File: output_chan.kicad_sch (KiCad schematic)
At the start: 12 parts, among them U4 MAX14917AFM+

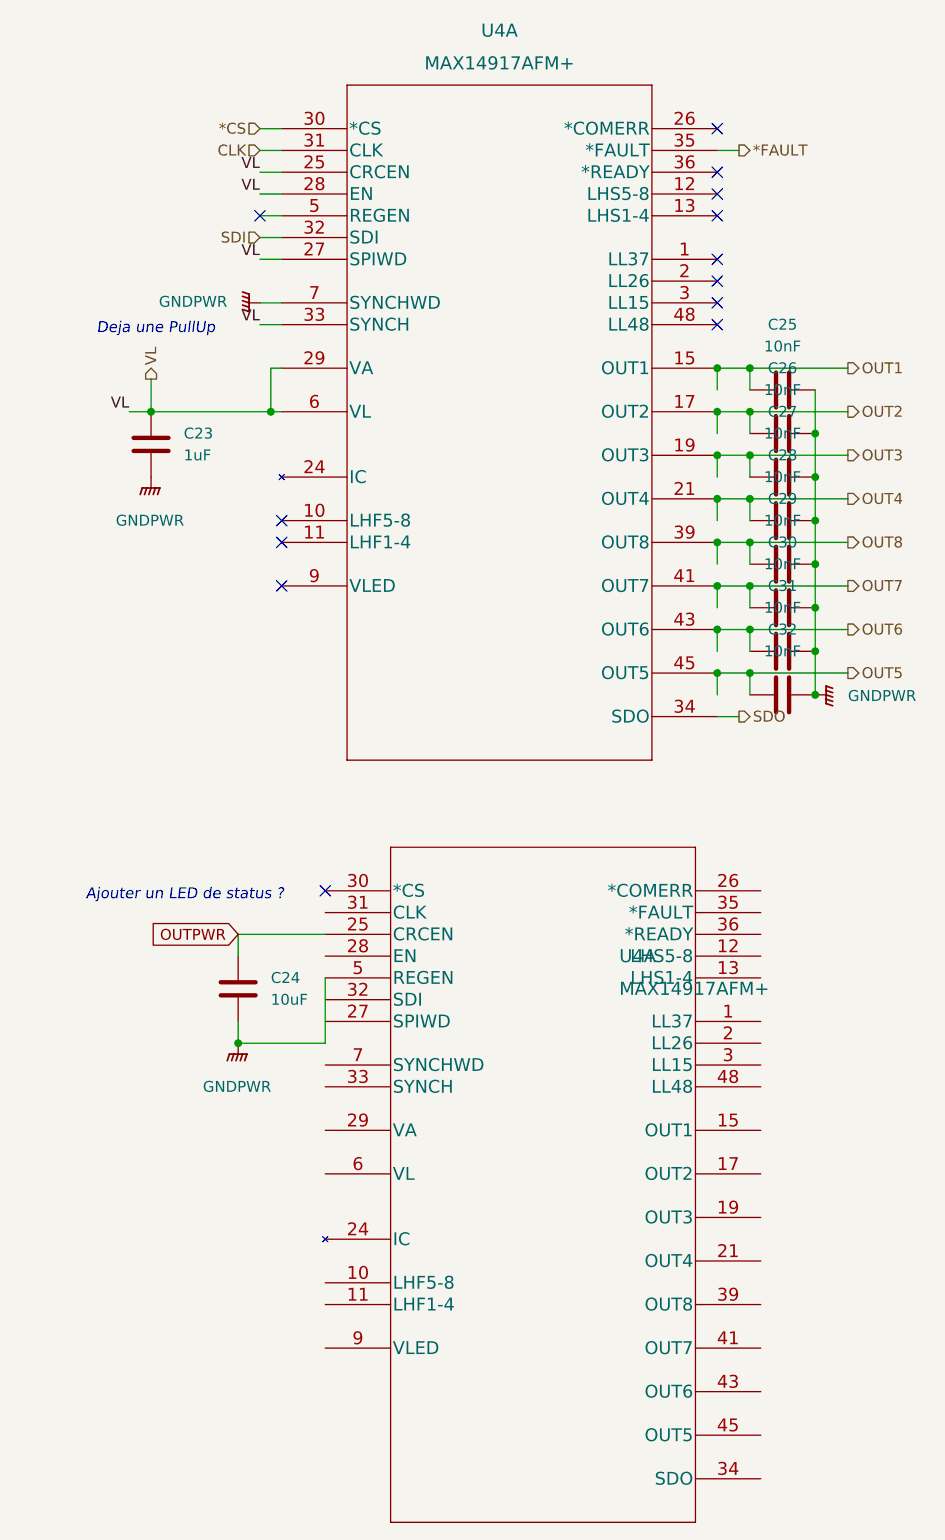
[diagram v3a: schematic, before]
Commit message: fixes after V1
4 resistors for input power
disable CRCEN
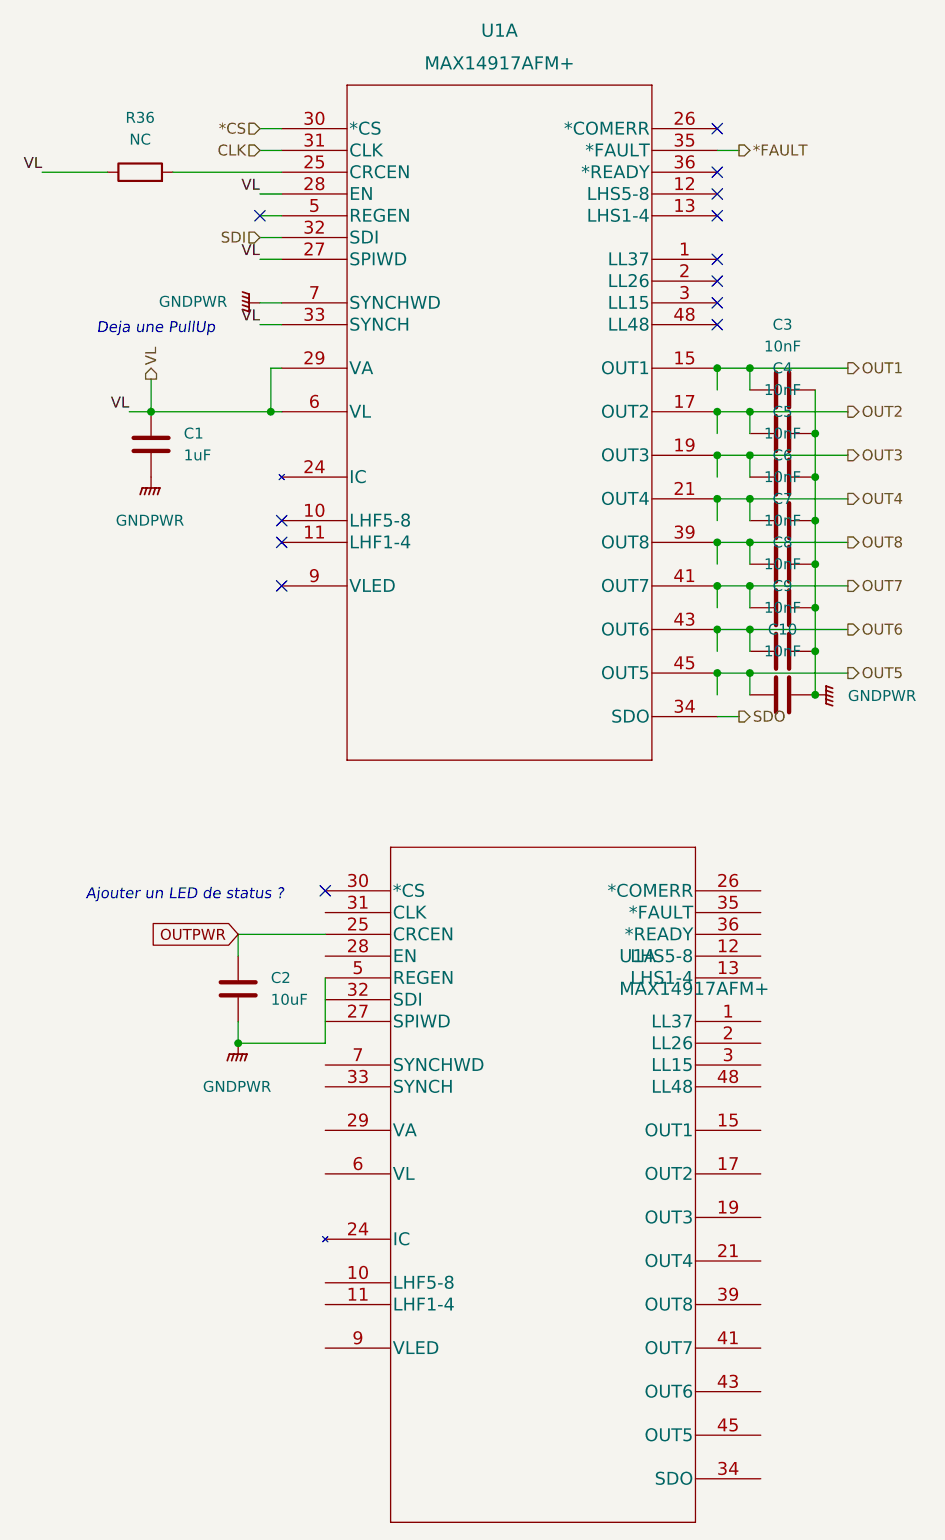
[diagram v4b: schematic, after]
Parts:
- added R36: NC, Resistor_SMD:R_0603_1608Metric, symbol Device:R
- renumbered C23 to C1, C32 to C10, C24 to C2, C25 to C3, C26 to C4, C27 to C5, C28 to C6, C29 to C7, C30 to C8, C31 to C9, U4 to U1
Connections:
- net VL: now also R36.1; no longer U1.25 (CRCEN)
- new net: R36.2, U1.25 (CRCEN)
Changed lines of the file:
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@@
+    (stroke (width 0) (type default) (color 0 0 0 0))
+  )
+  (wire (pts (xy 99.06 48.26) (xy 106.68 48.26))
     (stroke (width 0) (type default) (color 0 0 0 0))
   )
@@
     (stroke (width 0) (type default) (color 0 0 0 0))
   )
+  (wire (pts (xy 114.3 48.26) (xy 127 48.26))
+    (stroke (width 0) (type default) (color 0 0 0 0))
+  )
   (wire (pts (xy 181.61 101.6) (xy 181.61 104.14))
     (stroke (width 0) (type default) (color 0 0 0 0))
@@
   )
   (wire (pts (xy 177.8 96.52) (xy 177.8 99.06))
-    (stroke (width 0) (type default) (color 0 0 0 0))
-  )
-  (wire (pts (xy 124.46 48.26) (xy 127 48.26))
     (stroke (width 0) (type default) (color 0 0 0 0))
   )
@@
     (effects (font (size 1.27 1.27)) (justify right bottom))
   )
-  (label "VL" (at 124.46 48.26 180)
+  (label "VL" (at 99.06 48.26 180)
     (effects (font (size 1.27 1.27)) (justify right bottom))
   )
@@
   (symbol (lib_id "Device:C") (at 111.76 80.01 0)
     (in_bom yes) (on_board yes) (fields_autoplaced)
-    (property "Reference" "C23" (id 0) (at 115.57 78.7399 0)
+    (property "Reference" "C1" (id 0) (at 115.57 78.7399 0)
       (effects (font (size 1.27 1.27)) (justify left))
     )
@@
   (symbol (lib_id "Maxim industrial IO:MAX14917AFM+") (at 127 43.18 0)
     (in_bom yes) (on_board yes) (fields_autoplaced)
-    (property "Reference" "U4" (id 0) (at 152.4 31.75 0)
+    (property "Reference" "U1" (id 0) (at 152.4 31.75 0)
       (effects (font (size 1.524 1.524)))
     )
@@
   (symbol (lib_id "Device:C") (at 185.42 83.82 90)
     (in_bom yes) (on_board yes) (fields_autoplaced)
-    (property "Reference" "C27" (id 0) (at 185.42 76.2 90))
+    (property "Reference" "C5" (id 0) (at 185.42 76.2 90))
     (property "Value" "10nF" (id 1) (at 185.42 78.74 90))
     (property "Footprint" "Capacitor_SMD:C_0603_1608Metric" (id 2) (at 189.23 82.8548 0)
@@
     (pin "2")
   )
+  (symbol (lib_id "Device:R") (at 110.49 48.26 90)
+    (in_bom yes) (on_board yes) (fields_autoplaced)
+    (property "Reference" "R36" (id 0) (at 110.49 41.91 90))
+    (property "Value" "NC" (id 1) (at 110.49 44.45 90))
+    (property "Footprint" "Resistor_SMD:R_0603_1608Metric" (id 2) (at 110.49 50.038 90)
+      (effects (font (size 1.27 1.27)) hide)
+    )
+    (property "Datasheet" "~" (id 3) (at 110.49 48.26 0)
+      (effects (font (size 1.27 1.27)) hide)
+    )
+    (pin "1")
+    (pin "2")
+  )
   (symbol (lib_id "Device:C") (at 185.42 88.9 90)
     (in_bom yes) (on_board yes) (fields_autoplaced)
-    (property "Reference" "C28" (id 0) (at 185.42 81.28 90))
+    (property "Reference" "C6" (id 0) (at 185.42 81.28 90))
     (property "Value" "10nF" (id 1) (at 185.42 83.82 90))
     (property "Footprint" "Capacitor_SMD:C_0603_1608Metric" (id 2) (at 189.23 87.9348 0)
@@
   (symbol (lib_id "Device:C") (at 185.42 78.74 90)
     (in_bom yes) (on_board yes) (fields_autoplaced)
-    (property "Reference" "C26" (id 0) (at 185.42 71.12 90))
+    (property "Reference" "C4" (id 0) (at 185.42 71.12 90))
     (property "Value" "10nF" (id 1) (at 185.42 73.66 90))
     (property "Footprint" "Capacitor_SMD:C_0603_1608Metric" (id 2) (at 189.23 77.7748 0)
@@
   (symbol (lib_id "Device:C") (at 185.42 104.14 90)
     (in_bom yes) (on_board yes) (fields_autoplaced)
-    (property "Reference" "C31" (id 0) (at 185.42 96.52 90))
+    (property "Reference" "C9" (id 0) (at 185.42 96.52 90))
     (property "Value" "10nF" (id 1) (at 185.42 99.06 90))
     (property "Footprint" "Capacitor_SMD:C_0603_1608Metric" (id 2) (at 189.23 103.1748 0)
@@
   (symbol (lib_id "Maxim industrial IO:MAX14917AFM+") (at 132.08 132.08 0)
     (in_bom yes) (on_board yes) (fields_autoplaced)
-    (property "Reference" "U4" (id 0) (at 166.37 139.7 0)
+    (property "Reference" "U1" (id 0) (at 166.37 139.7 0)
       (effects (font (size 1.524 1.524)) (justify left))
     )
@@
   (symbol (lib_id "Device:C") (at 185.42 93.98 90)
     (in_bom yes) (on_board yes) (fields_autoplaced)
-    (property "Reference" "C29" (id 0) (at 185.42 86.36 90))
+    (property "Reference" "C7" (id 0) (at 185.42 86.36 90))
     (property "Value" "10nF" (id 1) (at 185.42 88.9 90))
     (property "Footprint" "Capacitor_SMD:C_0603_1608Metric" (id 2) (at 189.23 93.0148 0)
@@
   (symbol (lib_id "Device:C") (at 185.42 73.66 90)
     (in_bom yes) (on_board yes) (fields_autoplaced)
-    (property "Reference" "C25" (id 0) (at 185.42 66.04 90))
+    (property "Reference" "C3" (id 0) (at 185.42 66.04 90))
     (property "Value" "10nF" (id 1) (at 185.42 68.58 90))
     (property "Footprint" "Capacitor_SMD:C_0603_1608Metric" (id 2) (at 189.23 72.6948 0)
@@
   (symbol (lib_id "Device:C") (at 185.42 99.06 90)
     (in_bom yes) (on_board yes) (fields_autoplaced)
-    (property "Reference" "C30" (id 0) (at 185.42 91.44 90))
+    (property "Reference" "C8" (id 0) (at 185.42 91.44 90))
     (property "Value" "10nF" (id 1) (at 185.42 93.98 90))
     (property "Footprint" "Capacitor_SMD:C_0603_1608Metric" (id 2) (at 189.23 98.0948 0)
@@
   (symbol (lib_id "Device:C") (at 121.92 143.51 0)
     (in_bom yes) (on_board yes) (fields_autoplaced)
-    (property "Reference" "C24" (id 0) (at 125.73 142.2399 0)
+    (property "Reference" "C2" (id 0) (at 125.73 142.2399 0)
       (effects (font (size 1.27 1.27)) (justify left))
     )
@@
   (symbol (lib_id "Device:C") (at 185.42 109.22 90)
     (in_bom yes) (on_board yes) (fields_autoplaced)
-    (property "Reference" "C32" (id 0) (at 185.42 101.6 90))
+    (property "Reference" "C10" (id 0) (at 185.42 101.6 90))
     (property "Value" "10nF" (id 1) (at 185.42 104.14 90))
     (property "Footprint" "Capacitor_SMD:C_0603_1608Metric" (id 2) (at 189.23 108.2548 0)
